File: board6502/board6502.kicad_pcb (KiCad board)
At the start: 2 copper layers, 100 x 100 mm, 52 parts, among them J1 IO Pinheader, J2 UART, J3 USB_B, J4 Expansion Port, J5 Power connector, M3 MountingHole_3.2mm_M3, SW1 Reset button, SW2 SW_NMI, U1 DS1813, U2 74LS00, U3 74LS04, U4 W65C22N, U5 74LS30, U6 W65C51N, U7 W65C02, U8 AT28C64B, U9 CY7C199, X1 1-10MHz, Y1 1.8432M

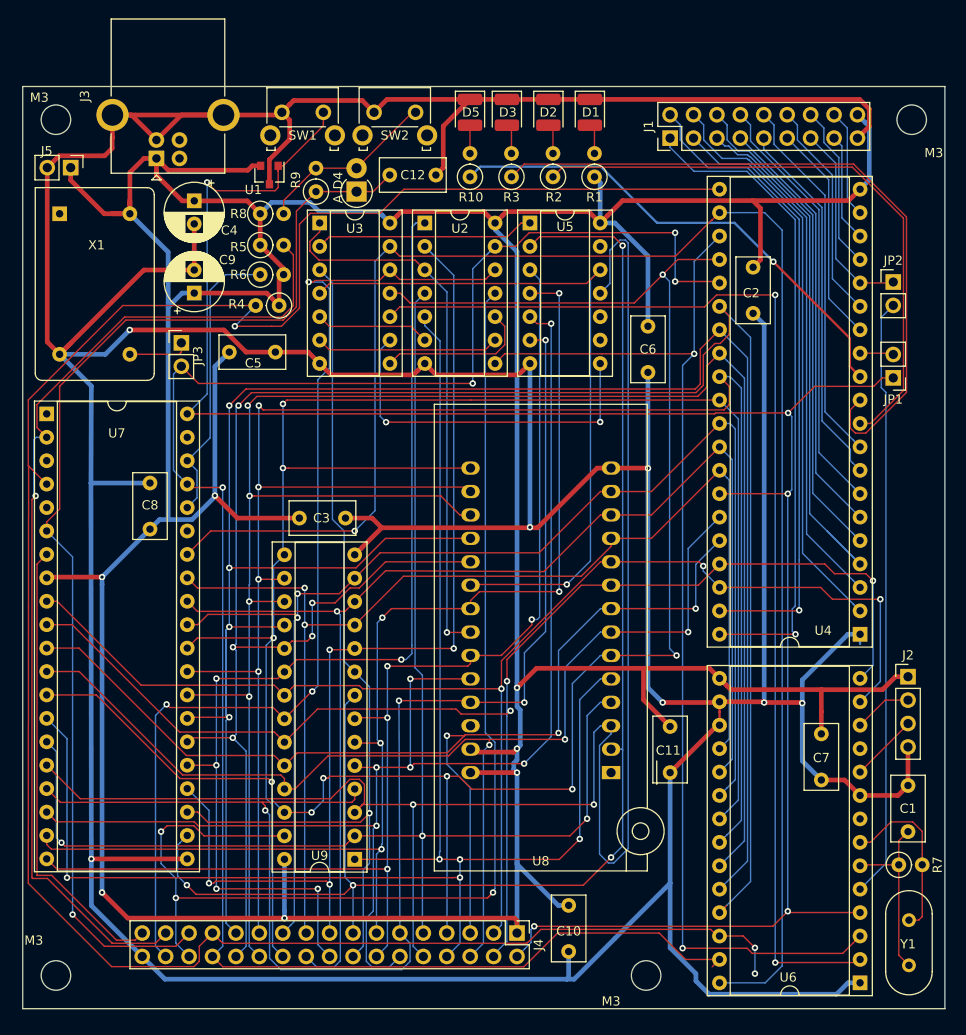
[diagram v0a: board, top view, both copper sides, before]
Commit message: add component annotation
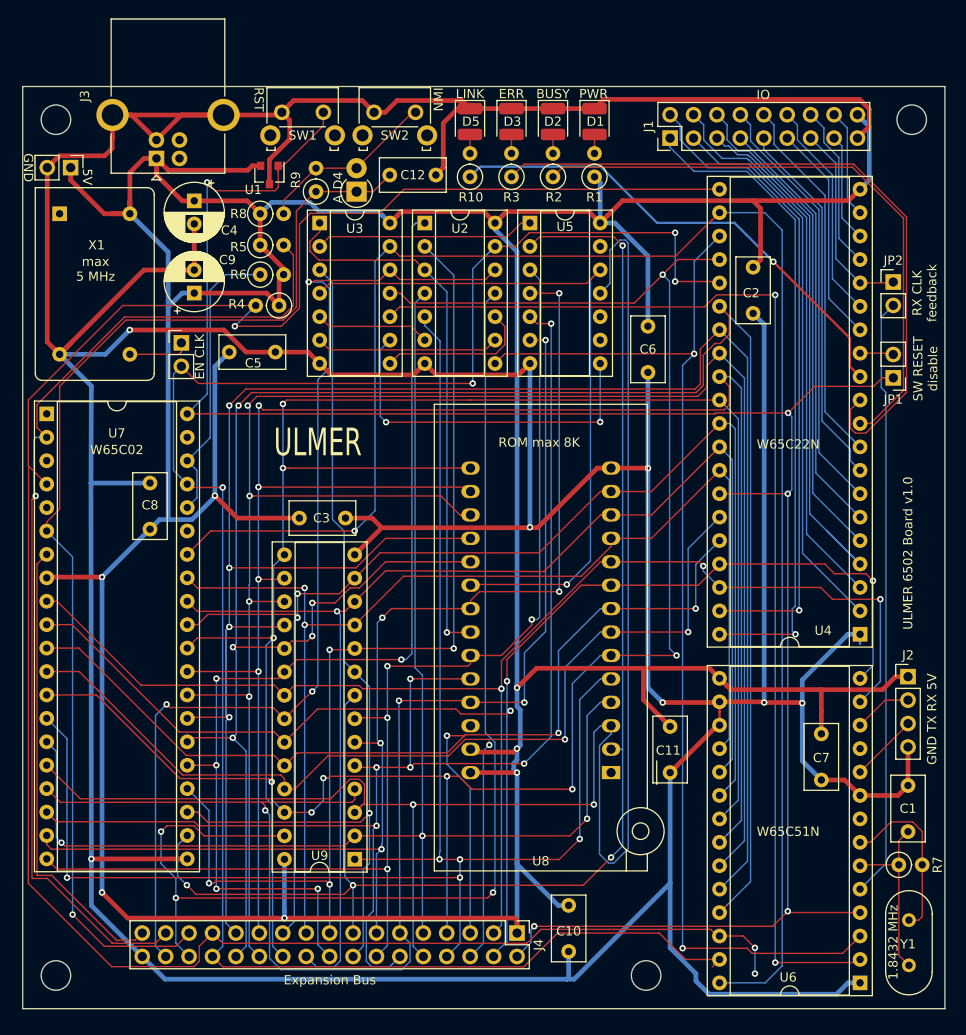
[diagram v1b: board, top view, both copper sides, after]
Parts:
- moved D1 1.12 mm to (107.0, 34.8)
- moved D2 1.12 mm to (102.5, 34.8)
- moved D3 1.12 mm to (98.0, 34.8)
- moved D5 1.00 mm to (93.5, 34.8)
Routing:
- net Net-(D5-Pad2): track 3.06 -> 2.06 mm
- net GND: track 630.3 -> 630.8 mm
- net Net-(D3-Pad2): track 3.27 -> 2.77 mm
- net Net-(D2-Pad2): track 3.27 -> 2.77 mm
- net Net-(D1-Pad2): track 3.27 -> 2.77 mm
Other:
- board text added: "1.8432 MHz"
- board text added: "5V"
- board text added: "BUSY"
- board text added: "EN CLK"
- board text added: "ERR"
- board text added: "Expansion Bus"
- board text added: "GND"
- board text added: "GND TX RX 5V"
- board text added: "IO"
- board text added: "LINK"
- board text added: "NMI"
- board text added: "PWR"
- board text added: "ROM max 8K"
- board text added: "RST"
- board text added: "RX CLK feedback"
- board text added: "SW RESET disable"
- board text added: "ULMER"
- board text added: "ULMER 6502 Board v1.0"
- board text added: "W65C02"
- board text added: "W65C22N"
- board text added: "W65C51N"
- board text added: "max 5 MHz"

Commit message: annotate expansion bus
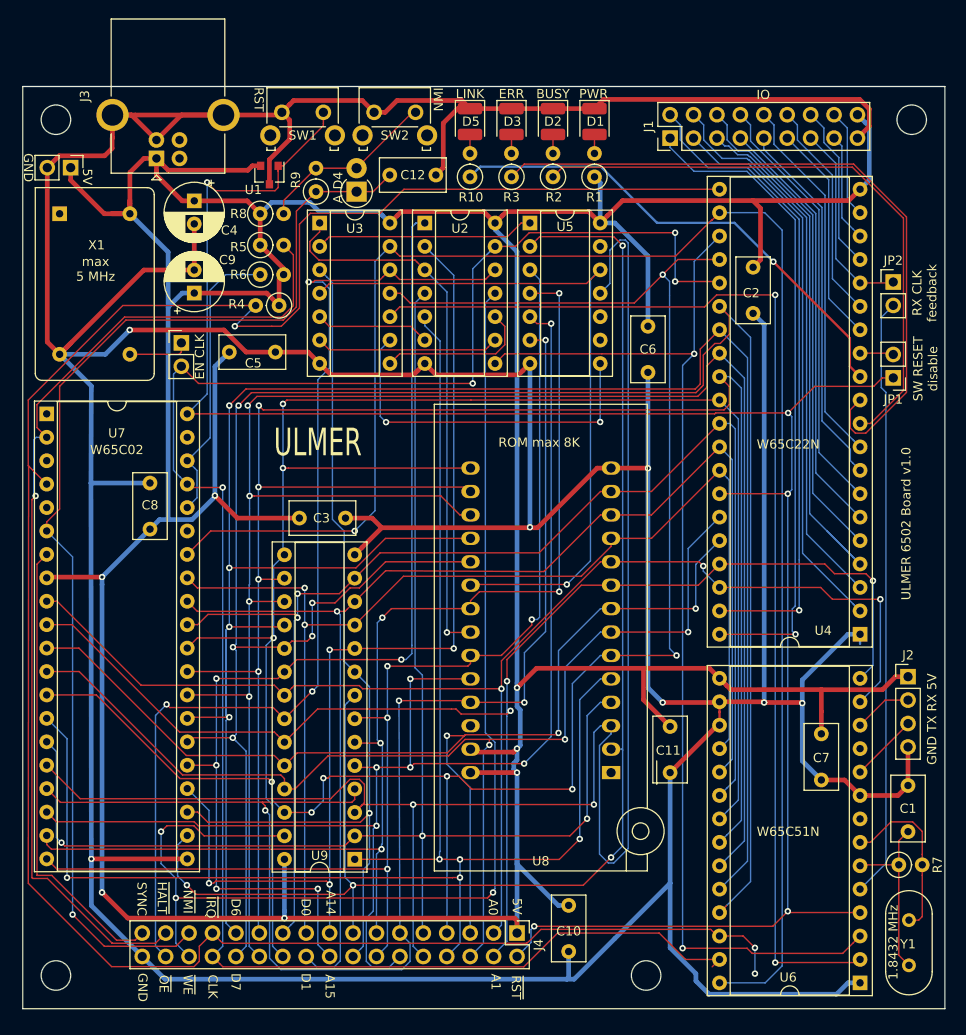
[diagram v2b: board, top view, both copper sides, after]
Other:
- board text added: "A0"
- board text added: "A1"
- board text added: "A14"
- board text added: "A15"
- board text added: "CLK"
- board text added: "D0"
- board text added: "D1"
- board text added: "D6"
- board text added: "D7"
- board text added: "SYNC"
- board text added: "~HALT"
- board text added: "~IRQ"
- board text added: "~NMI"
- board text added: "~OE"
- board text added: "~RST"
- board text added: "~WE"
- board text removed: "Expansion Bus"
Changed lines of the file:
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@@
   (general
     (thickness 1.6)
-    (drawings 33)
+    (drawings 50)
     (tracks 1505)
     (zones 0)
@@
     )
   )
+  (gr_text ~IRQ (at 65.4 120 270) (layer F.SilkS)
+    (effects (font (size 1 1) (thickness 0.15)))
+  )
+  (gr_text SYNC (at 57.9 119.1 270) (layer F.SilkS)
+    (effects (font (size 1 1) (thickness 0.15)))
+  )
+  (gr_text ~HALT (at 60.1 119 270) (layer F.SilkS)
+    (effects (font (size 1 1) (thickness 0.15)))
+  )
+  (gr_text ~NMI (at 62.9 119.4 270) (layer F.SilkS)
+    (effects (font (size 1 1) (thickness 0.15)))
+  )
+  (gr_text ~OE (at 60.3 128.3 270) (layer F.SilkS)
+    (effects (font (size 1 1) (thickness 0.15)))
+  )
+  (gr_text ~WE (at 62.9 128.4 270) (layer F.SilkS)
+    (effects (font (size 1 1) (thickness 0.15)))
+  )
+  (gr_text CLK (at 65.6 128.6 270) (layer F.SilkS)
+    (effects (font (size 1 1) (thickness 0.15)))
+  )
+  (gr_text D6 (at 68.1 120 270) (layer F.SilkS)
+    (effects (font (size 1 1) (thickness 0.15)))
+  )
+  (gr_text D7 (at 68.1 128.1 270) (layer F.SilkS)
+    (effects (font (size 1 1) (thickness 0.15)))
+  )
+  (gr_text "A14\n" (at 78.4 119.5 270) (layer F.SilkS)
+    (effects (font (size 1 1) (thickness 0.15)))
+  )
+  (gr_text D0 (at 75.7 120 270) (layer F.SilkS)
+    (effects (font (size 1 1) (thickness 0.15)))
+  )
+  (gr_text D1 (at 75.7 128.1 270) (layer F.SilkS)
+    (effects (font (size 1 1) (thickness 0.15)))
+  )
+  (gr_text A15 (at 78.3 128.6 270) (layer F.SilkS)
+    (effects (font (size 1 1) (thickness 0.15)))
+  )
+  (gr_text A1 (at 96.3 128.1 270) (layer F.SilkS)
+    (effects (font (size 1 1) (thickness 0.15)))
+  )
+  (gr_text A0 (at 96 120 270) (layer F.SilkS)
+    (effects (font (size 1 1) (thickness 0.15)))
+  )
+  (gr_text ~RST (at 98.5 128.7 270) (layer F.SilkS)
+    (effects (font (size 1 1) (thickness 0.15)))
+  )
+  (gr_text 5V (at 98.6 119.9 270) (layer F.SilkS)
+    (effects (font (size 1 1) (thickness 0.15)))
+  )
+  (gr_text GND (at 58 128.7 270) (layer F.SilkS)
+    (effects (font (size 1 1) (thickness 0.15)))
+  )
   (gr_text "EN CLK" (at 64.2 60.3 90) (layer F.SilkS)
     (effects (font (size 1 1) (thickness 0.15)))
@@
     (effects (font (size 1 1) (thickness 0.15)))
   )
-  (gr_text "Expansion Bus" (at 78.3 127.9) (layer F.SilkS)
-    (effects (font (size 1 1) (thickness 0.15)))
-  )
   (gr_text "max\n5 MHz" (at 52.9 50.8) (layer F.SilkS)
     (effects (font (size 1 1) (thickness 0.15)))
@@
     (effects (font (size 1 1) (thickness 0.15)))
   )
-  (gr_text "ULMER 6502 Board v1.0" (at 141 81.6 90) (layer F.SilkS)
+  (gr_text "ULMER 6502 Board v1.0" (at 140.8 78.4 90) (layer F.SilkS)
     (effects (font (size 1 1) (thickness 0.15)))
   )
